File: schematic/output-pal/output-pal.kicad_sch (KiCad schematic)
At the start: 43 parts, among them J1 Conn_01x08_Pin, J3 Conn_01x02_Pin, SW1 SW_DIP_x02, U1 LM555xN, U4 AT28C64B-15PC, U5 HDSP-7503, U6 HDSP-7503, U7 HDSP-7503, U8 HDSP-7503, U9 GAL16V8

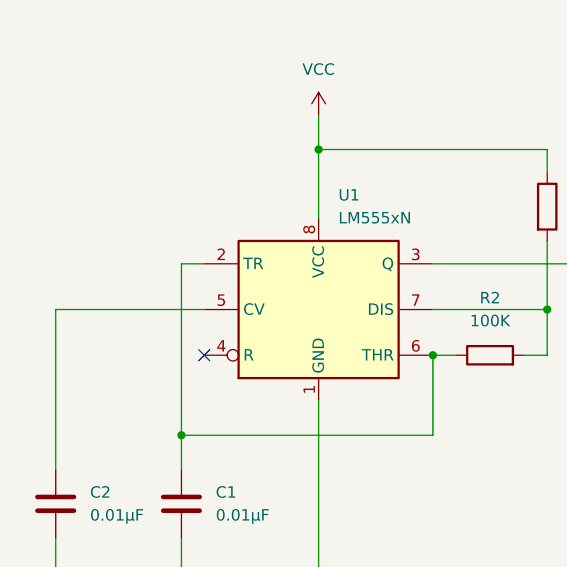
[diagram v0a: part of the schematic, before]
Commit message: New release of output.
Improved layout (more compact)
Bigger LEDs
More SMD components (including 7555 and capacitors)
Front copper fill
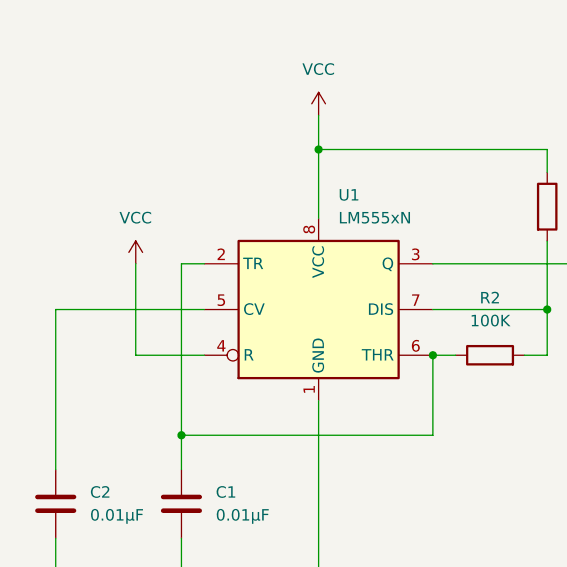
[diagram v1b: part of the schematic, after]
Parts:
- C1, C2: footprint Capacitor_THT:C_Rect_L4.0mm_W2.5mm_P2.50mm -> Capacitor_SMD:C_1206_3216Metric_Pad1.33x1.80mm_HandSolder
- D1, D2, D3, D4, D5, D6, D7, D8: footprint Capacitor_SMD:C_0603_1608Metric_Pad1.08x0.95mm_HandSolder -> Capacitor_SMD:C_0805_2012Metric_Pad1.18x1.45mm_HandSolder
- U1: footprint Package_DIP:DIP-8_W7.62mm -> Package_SO:SOIC-8_3.9x4.9mm_P1.27mm
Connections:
- net VCC: now also U1.4 (R)
- no-connect marks 11 -> 10
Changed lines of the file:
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@@
 		(title "Output Display Module")
 		(date "2024-05-12")
-		(rev "2.0")
+		(rev "2.1")
 		(company "Silicon Chronicles")
 	)
@@
 	)
 	(no_connect
-		(at 34.29 59.69)
-	)
-	(no_connect
 		(at 120.65 34.29)
 	)
@@
 	(wire
 		(pts
+			(xy 26.67 49.53) (xy 26.67 59.69)
+		)
+		(stroke
+			(width 0)
+			(type default)
+		)
+	)
+	(wire
+		(pts
 			(xy 74.93 119.38) (xy 77.47 119.38)
 		)
@@
 		)
 	)
+	(wire
+		(pts
+			(xy 26.67 59.69) (xy 34.29 59.69)
+		)
+		(stroke
+			(width 0)
+			(type default)
+		)
+	)
 	(bus
 		(pts
@@
 			)
 		)
-		(property "Footprint" "Capacitor_SMD:C_0603_1608Metric_Pad1.08x0.95mm_HandSolder"
+		(property "Footprint" "Capacitor_SMD:C_0805_2012Metric_Pad1.18x1.45mm_HandSolder"
 			(at 146.05 171.45 0)
 			(effects
@@
 			)
 		)
-		(property "Footprint" "Capacitor_SMD:C_0603_1608Metric_Pad1.08x0.95mm_HandSolder"
+		(property "Footprint" "Capacitor_SMD:C_0805_2012Metric_Pad1.18x1.45mm_HandSolder"
 			(at 146.05 173.99 0)
 			(effects
@@
 			)
 		)
-		(property "Footprint" "Capacitor_THT:C_Rect_L4.0mm_W2.5mm_P2.50mm"
+		(property "Footprint" "Capacitor_SMD:C_1206_3216Metric_Pad1.33x1.80mm_HandSolder"
 			(at 18.7452 80.01 0)
 			(effects
@@
 			)
 		)
-		(property "Footprint" "Capacitor_SMD:C_0603_1608Metric_Pad1.08x0.95mm_HandSolder"
+		(property "Footprint" "Capacitor_SMD:C_0805_2012Metric_Pad1.18x1.45mm_HandSolder"
 			(at 146.05 184.15 0)
 			(effects
@@
 	)
 	(symbol
+		(lib_id "power:VCC")
+		(at 26.67 49.53 0)
+		(unit 1)
+		(exclude_from_sim no)
+		(in_bom yes)
+		(on_board yes)
+		(dnp no)
+		(fields_autoplaced yes)
+		(property "Reference" "#PWR015"
+			(at 26.67 53.34 0)
+			(effects
+				(font
+					(size 1.27 1.27)
+				)
+				(hide yes)
+			)
+		)
+		(property "Value" "VCC"
+			(at 26.67 44.45 0)
+			(effects
+				(font
+					(size 1.27 1.27)
+				)
+			)
+		)
+		(property "Footprint" ""
+			(at 26.67 49.53 0)
+			(effects
+				(font
+					(size 1.27 1.27)
+				)
+				(hide yes)
+			)
+		)
+		(property "Datasheet" ""
+			(at 26.67 49.53 0)
+			(effects
+				(font
+					(size 1.27 1.27)
+				)
+				(hide yes)
+			)
+		)
+		(property "Description" "Power symbol creates a global label with name \"VCC\""
+			(at 26.67 49.53 0)
+			(effects
+				(font
+					(size 1.27 1.27)
+				)
+				(hide yes)
+			)
+		)
+		(pin "1"
+		)
+		(instances
+			(project "output-pal"
+				(path "/20d0a6e4-c08e-4125-9e51-8c0137e73b4f"
+					(reference "#PWR015")
+					(unit 1)
+				)
+			)
+		)
+	)
+	(symbol
 		(lib_id "Display_Character:HDSP-7503")
 		(at 215.9 111.76 0)
@@
 			)
 		)
-		(property "Footprint" "Capacitor_SMD:C_0603_1608Metric_Pad1.08x0.95mm_HandSolder"
+		(property "Footprint" "Capacitor_SMD:C_0805_2012Metric_Pad1.18x1.45mm_HandSolder"
 			(at 146.05 181.61 0)
 			(effects
@@
 			)
 		)
-		(property "Footprint" "Capacitor_SMD:C_0603_1608Metric_Pad1.08x0.95mm_HandSolder"
+		(property "Footprint" "Capacitor_SMD:C_0805_2012Metric_Pad1.18x1.45mm_HandSolder"
 			(at 146.05 179.07 0)
 			(effects
@@
 			)
 		)
-		(property "Footprint" "Capacitor_SMD:C_0603_1608Metric_Pad1.08x0.95mm_HandSolder"
+		(property "Footprint" "Capacitor_SMD:C_0805_2012Metric_Pad1.18x1.45mm_HandSolder"
 			(at 146.05 168.91 0)
 			(effects
@@
 			)
 		)
-		(property "Footprint" "Capacitor_SMD:C_0603_1608Metric_Pad1.08x0.95mm_HandSolder"
+		(property "Footprint" "Capacitor_SMD:C_0805_2012Metric_Pad1.18x1.45mm_HandSolder"
 			(at 146.05 176.53 0)
 			(effects
@@
 			)
 		)
-		(property "Footprint" "Capacitor_THT:C_Rect_L4.0mm_W2.5mm_P2.50mm"
+		(property "Footprint" "Capacitor_SMD:C_1206_3216Metric_Pad1.33x1.80mm_HandSolder"
 			(at 32.7152 80.01 0)
 			(effects
@@
 			)
 		)
-		(property "Footprint" "Capacitor_SMD:C_0603_1608Metric_Pad1.08x0.95mm_HandSolder"
+		(property "Footprint" "Capacitor_SMD:C_0805_2012Metric_Pad1.18x1.45mm_HandSolder"
 			(at 146.05 186.69 0)
 			(effects
@@
 			)
 		)
-		(property "Footprint" "Package_DIP:DIP-8_W7.62mm"
+		(property "Footprint" "Package_SO:SOIC-8_3.9x4.9mm_P1.27mm"
 			(at 63.5 64.77 0)
 			(effects
